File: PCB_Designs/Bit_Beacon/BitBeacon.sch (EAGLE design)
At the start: 105 parts, among them IC1 AD8603UJ, IC2 AD8603UJ, IC3 AD8603UJ, IC4 AD8603UJ

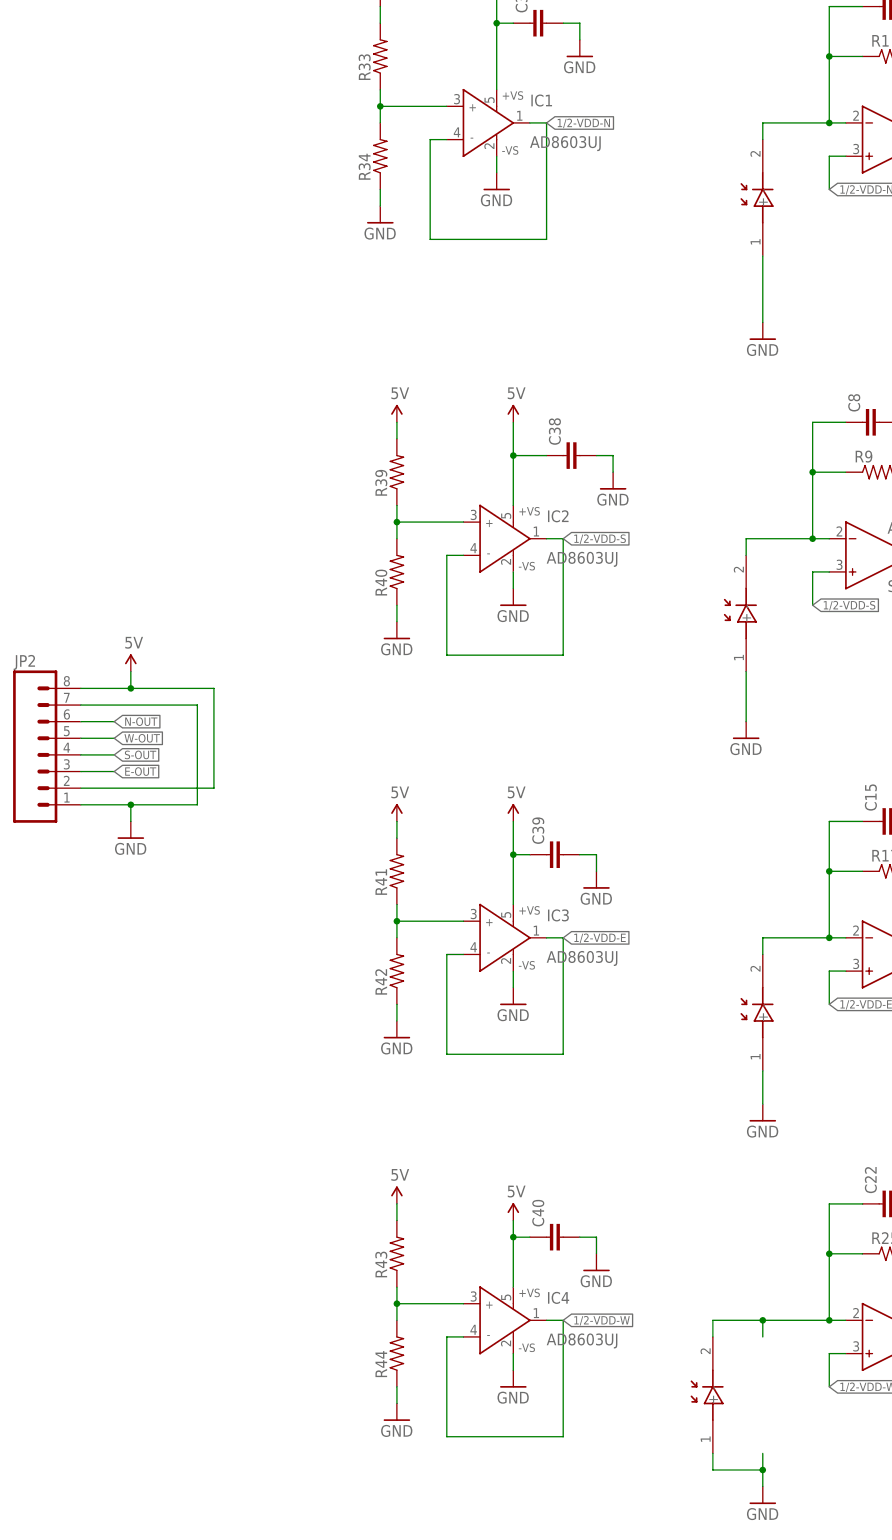
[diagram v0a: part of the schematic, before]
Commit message: finished and ordered PCB design for Bit Beacon
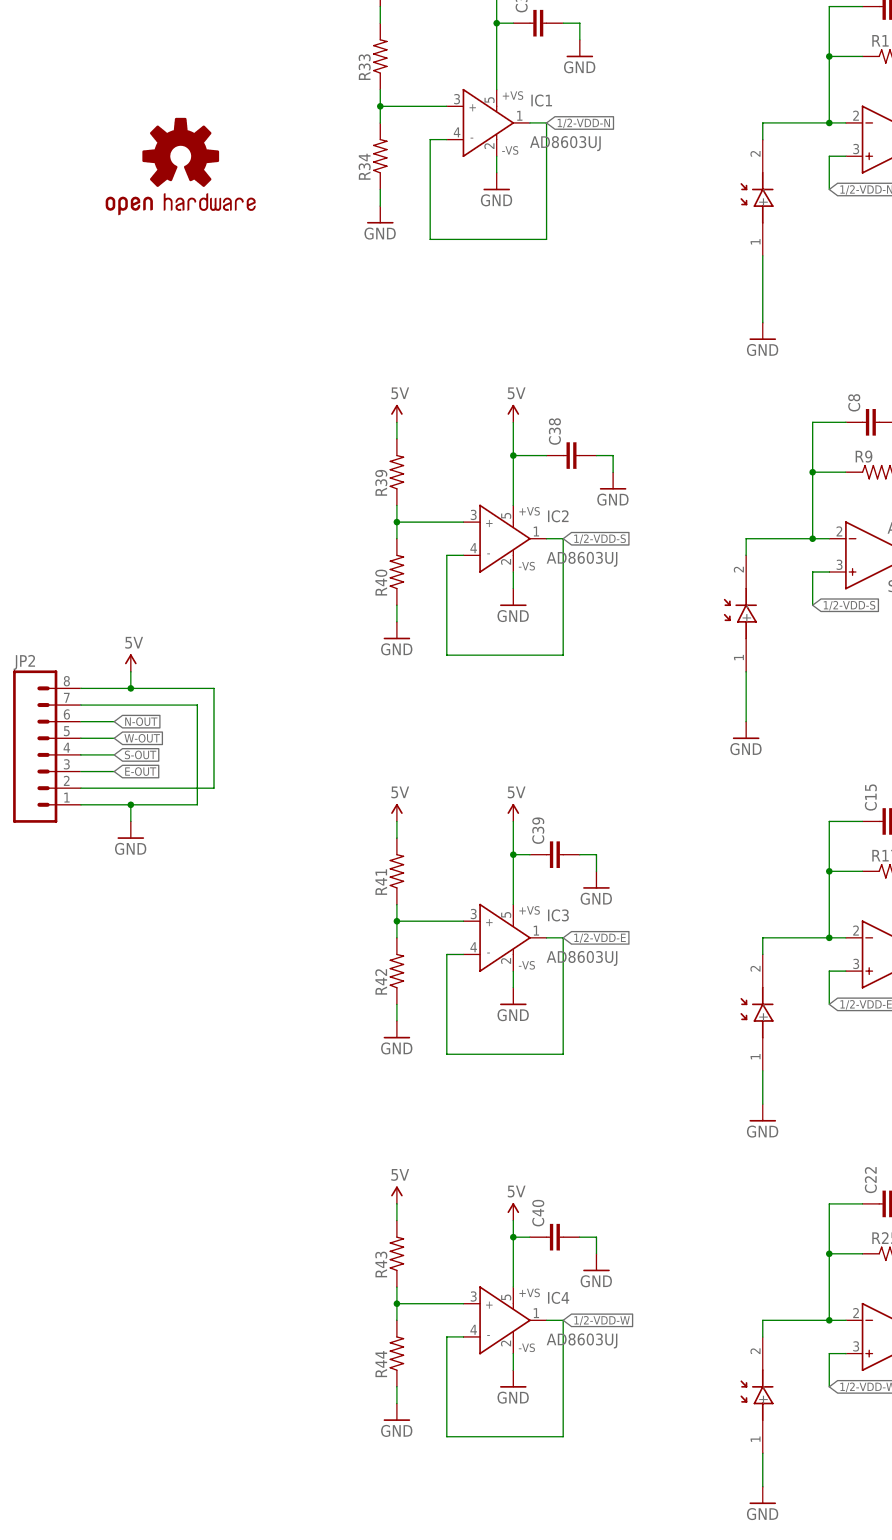
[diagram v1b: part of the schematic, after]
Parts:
- added LOGO1: OSHW-LOGOS, SparkFun-Aesthetics:OSHW-LOGOS
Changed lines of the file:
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@@
 <part name="C40" library="resistor" deviceset="C-EU" device="C0402"/>
 <part name="GND37" library="SparkFun-Aesthetics" deviceset="GND" device=""/>
+<part name="LOGO1" library="SparkFun-Aesthetics" deviceset="OSHW-LOGO" device="S"/>
 </parts>
 <sheets>
@@
 <instance part="S-PD1" gate="G$1" x="-20.32" y="30.48" rot="R90"/>
 <instance part="E-PD1" gate="G$1" x="-17.78" y="-30.48" rot="R90"/>
-<instance part="W-PD1" gate="G$1" x="-25.4" y="-88.9" rot="R90"/>
+<instance part="W-PD1" gate="G$1" x="-17.78" y="-88.9" rot="R90"/>
 <instance part="C33" gate="G$1" x="99.06" y="99.06" rot="R90"/>
 <instance part="R35" gate="G$1" x="106.68" y="91.44" rot="R90"/>
@@
 <instance part="C40" gate="G$1" x="-50.8" y="-63.5" rot="R90"/>
 <instance part="GND37" gate="1" x="-43.18" y="-68.58"/>
+<instance part="LOGO1" gate="G$1" x="-106.68" y="101.6"/>
 </instances>
 <busses>
@@
 <segment>
 <pinref part="GND6" gate="1" pin="GND"/>
-<wire x1="-17.78" y1="-101.6" x2="-17.78" y2="-99.06" width="0.1524" layer="91"/>
 <pinref part="W-PD1" gate="G$1" pin="+"/>
-<wire x1="-17.78" y1="-99.06" x2="-17.78" y2="-96.52" width="0.1524" layer="91"/>
-<wire x1="-25.4" y1="-96.52" x2="-25.4" y2="-99.06" width="0.1524" layer="91"/>
-<wire x1="-25.4" y1="-99.06" x2="-17.78" y2="-99.06" width="0.1524" layer="91"/>
-<junction x="-17.78" y="-99.06"/>
+<wire x1="-17.78" y1="-96.52" x2="-17.78" y2="-101.6" width="0.1524" layer="91"/>
 </segment>
 <segment>
@@
 <wire x1="-5.08" y1="-76.2" x2="-7.62" y2="-76.2" width="0.1524" layer="91"/>
 <wire x1="-7.62" y1="-76.2" x2="-17.78" y2="-76.2" width="0.1524" layer="91"/>
-<wire x1="-17.78" y1="-76.2" x2="-17.78" y2="-78.74" width="0.1524" layer="91"/>
 <pinref part="R25" gate="G$1" pin="1"/>
 <wire x1="-2.54" y1="-66.04" x2="-7.62" y2="-66.04" width="0.1524" layer="91"/>
@@
 <junction x="-7.62" y="-66.04"/>
 <pinref part="W-PD1" gate="G$1" pin="-"/>
-<wire x1="-25.4" y1="-78.74" x2="-25.4" y2="-76.2" width="0.1524" layer="91"/>
-<wire x1="-25.4" y1="-76.2" x2="-17.78" y2="-76.2" width="0.1524" layer="91"/>
-<junction x="-17.78" y="-76.2"/>
-</segment>
-</net>
+<wire x1="-17.78" y1="-78.74" x2="-17.78" y2="-76.2" width="0.1524" layer="91"/>
+</segment>
+</net>

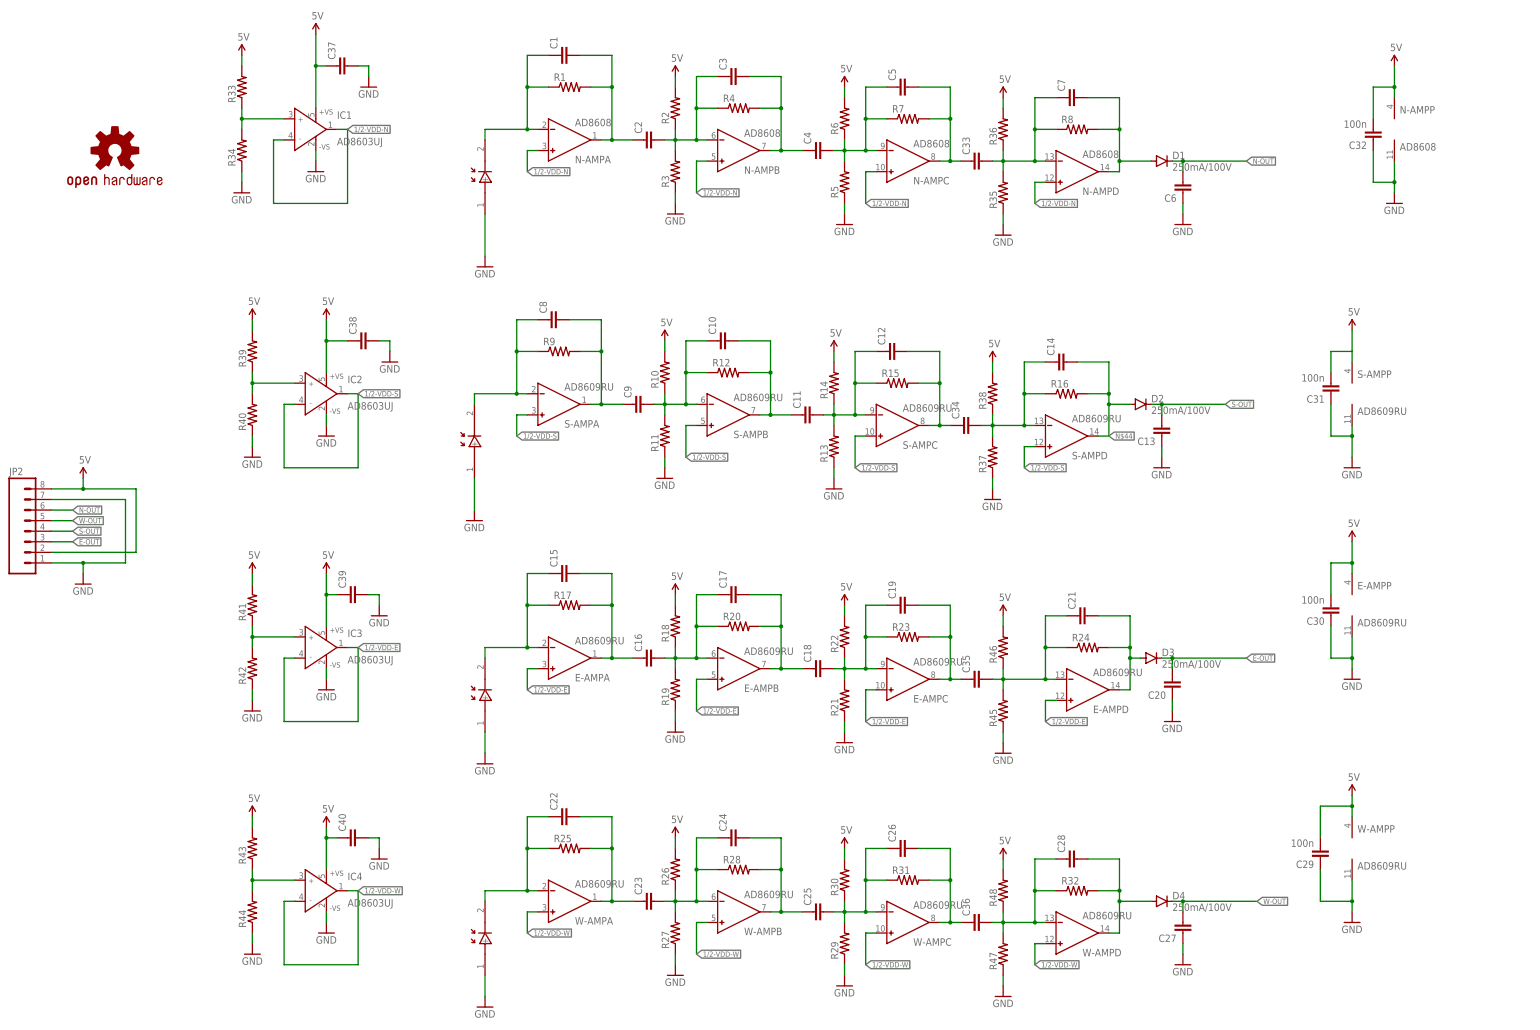
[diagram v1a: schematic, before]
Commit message: updating BitBeacon design with a better high pass filter design and started teh BitBeacon_Emitter circuit
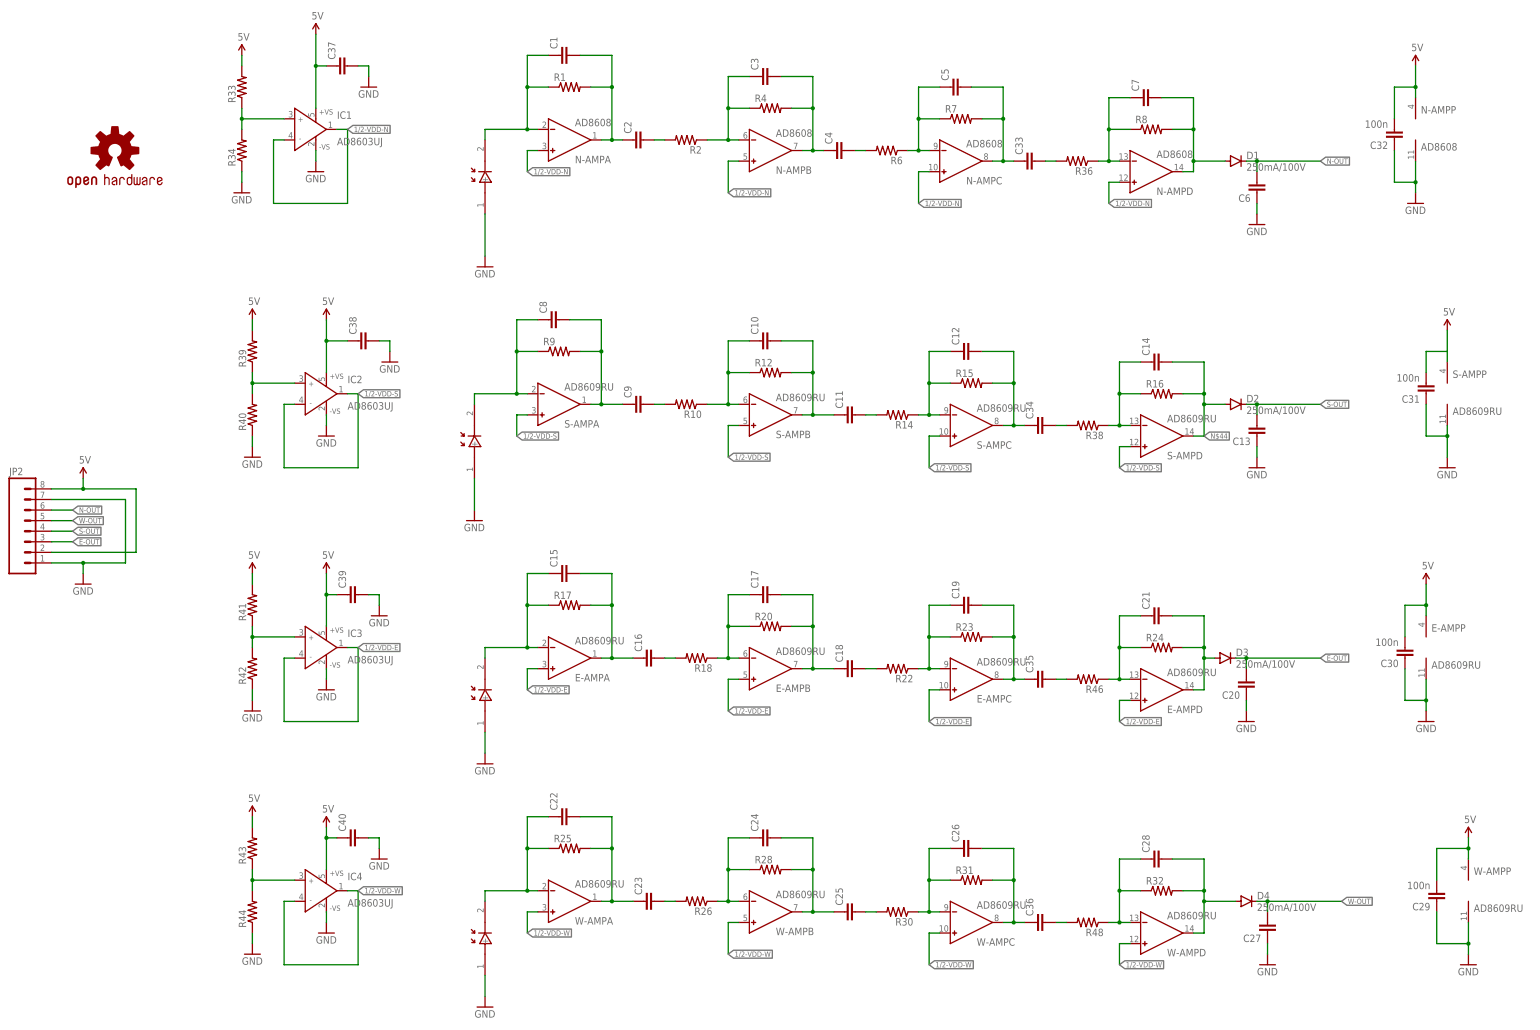
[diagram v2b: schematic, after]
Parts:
- removed R11, R13, R19, R21, R27, R29, R3, R35, R37, R45, R47, R5: (no value), resistor:R-US_R0402
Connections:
- new net N$27: C2.2, R2.2
- new net N$34: C4.2, R6.2
- new net N$35: C33.2, R36.2
- new net N$36: C34.2, R38.2
- new net N$37: C11.2, R14.2
- new net N$38: C9.2, R10.2
- new net N$39: C35.2, R46.2
- new net N$40: C18.2, R22.2
- new net N$41: C16.2, R18.2
- new net N$42: C36.2, R48.2
- new net N$43: C25.2, R30.2
- new net N$45: C23.2, R26.2
- net 5V: no longer R10.2, R14.2, R18.2, R2.2, R22.2, R26.2, R30.2, R36.2, R38.2, R46.2, R48.2, R6.2
- net GND: no longer R11.1, R13.1, R19.1, R21.1, R27.1, R29.1, R3.1, R35.1, R37.1, R45.1, R47.1, R5.1
- net N$10: no longer C33.2, R35.2
- net N$12: no longer C9.2, R11.2
- net N$14: no longer C11.2, R13.2
- net N$2: no longer C34.2, R37.2
- net N$21: no longer C16.2, R19.2
- net N$23: no longer C18.2, R21.2
- net N$25: no longer C36.2, R47.2
- net N$26: no longer C35.2, R45.2
- net N$30: no longer C23.2, R27.2
- net N$32: no longer C25.2, R29.2
- net N$5: no longer C2.2, R3.2
- net N$7: no longer C4.2, R5.2
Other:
- moved on the sheet: C10, C11, C12, C13, C14, C17, C18, C19, C2, C20, C21, C24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
